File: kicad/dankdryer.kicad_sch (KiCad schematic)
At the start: 22 parts, among them J13 barreljack, J9 UART, SW2 boot, U1 AP63203WU, U6 ESP32-C6-MINI-1U

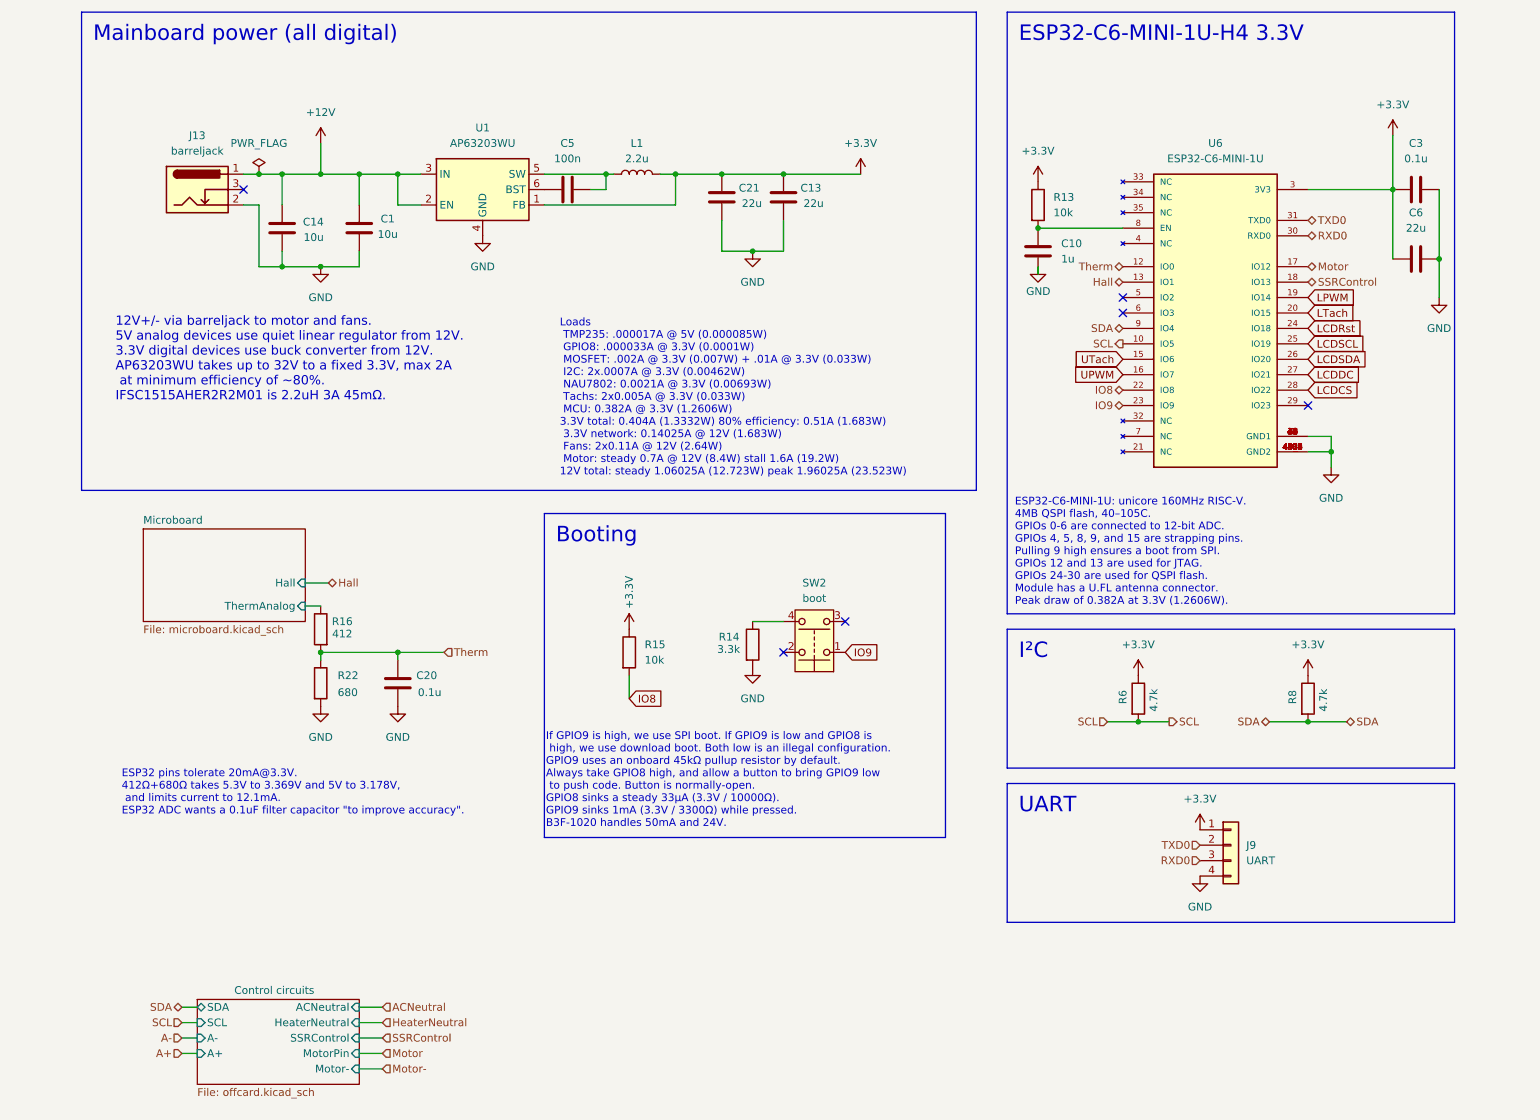
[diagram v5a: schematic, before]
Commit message: [pcb] don't run trace between connectors #97
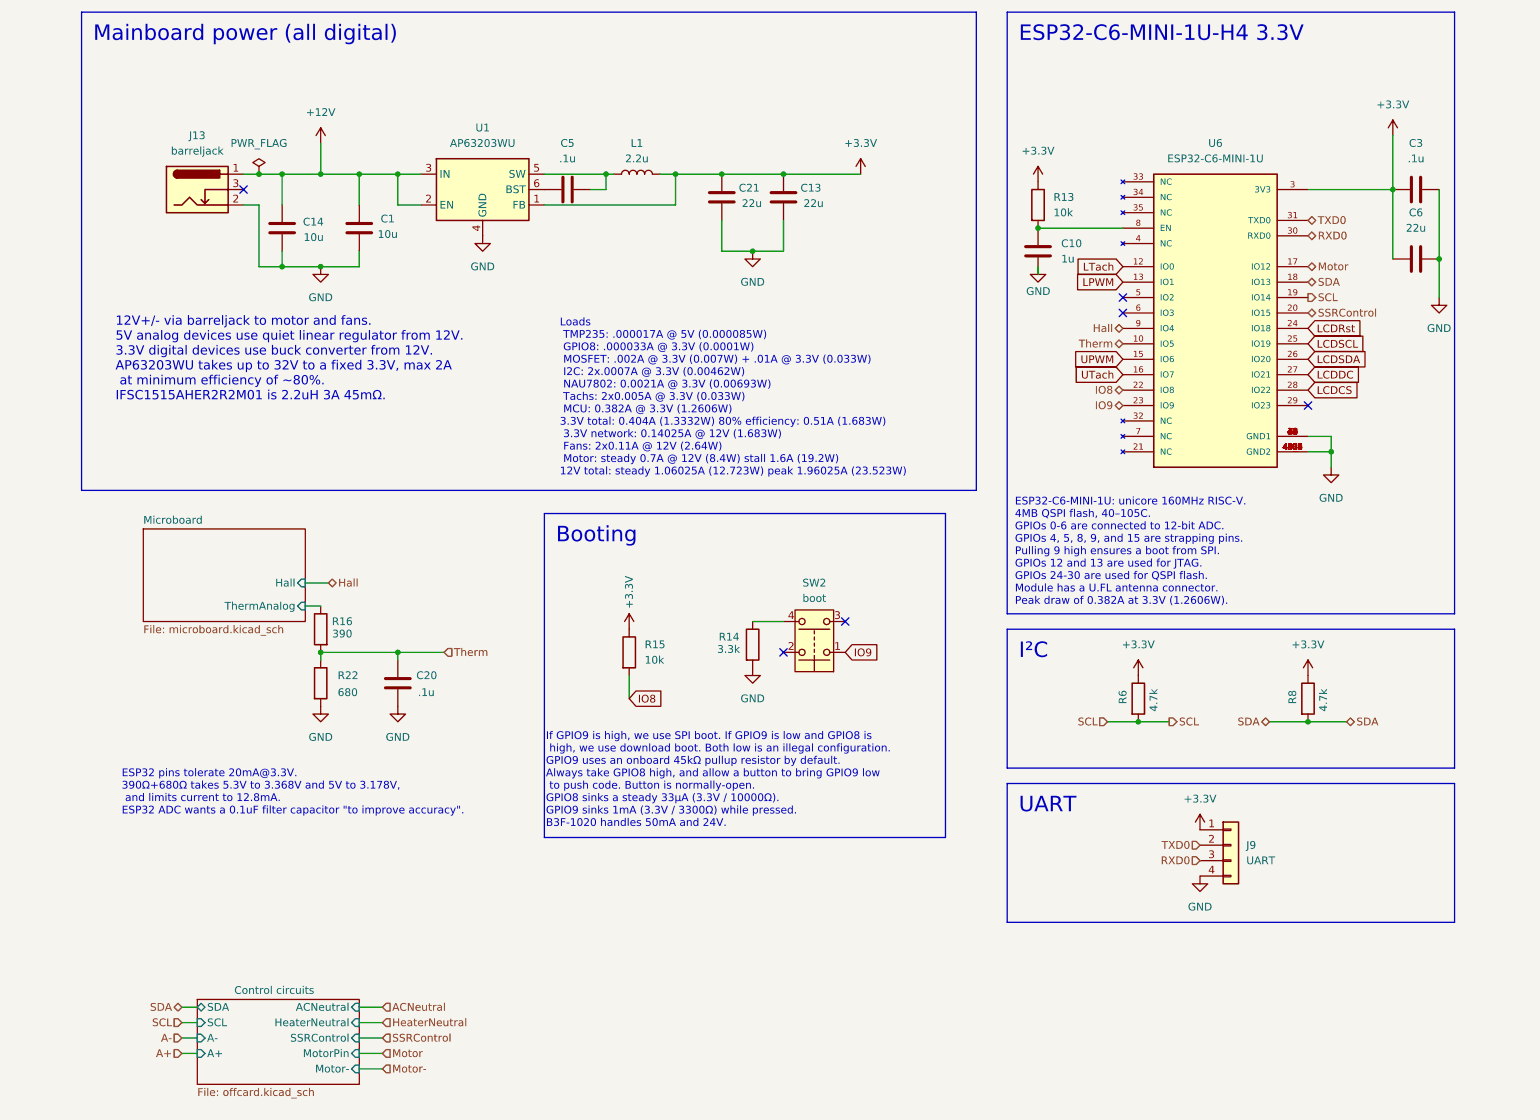
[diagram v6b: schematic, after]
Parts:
- C10, C6: footprint Capacitor_SMD:C_1206_3216Metric_Pad1.33x1.80mm_HandSolder -> Capacitor_SMD:C_0805_2012Metric_Pad1.18x1.45mm_HandSolder
- C20, C3: value 0.1u -> .1u; footprint Capacitor_SMD:C_1206_3216Metric_Pad1.33x1.80mm_HandSolder -> Capacitor_SMD:C_0805_2012Metric_Pad1.18x1.45mm_HandSolder
- C5: value 100n -> .1u
- R13, R22, R6, R8: footprint Resistor_SMD:R_1206_3216Metric_Pad1.30x1.75mm_HandSolder -> Resistor_SMD:R_0805_2012Metric_Pad1.20x1.40mm_HandSolder
- R16: value 412 -> 390; footprint Resistor_SMD:R_1206_3216Metric_Pad1.30x1.75mm_HandSolder -> Resistor_SMD:R_0805_2012Metric_Pad1.20x1.40mm_HandSolder
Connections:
- net Hall: now also U6.9 (IO4); no longer U6.13 (IO1)
- net LPWM: now also U6.13 (IO1); no longer U6.19 (IO14)
- net LTach: now also U6.12 (IO0); no longer U6.20 (IO15)
- net SCL: now also U6.19 (IO14); no longer U6.10 (IO5)
- net SDA: now also U6.18 (IO13); no longer U6.9 (IO4)
- net SSRControl: now also U6.20 (IO15); no longer U6.18 (IO13)
- net Therm: now also U6.10 (IO5); no longer U6.12 (IO0)
- net UPWM: now also U6.15 (IO6); no longer U6.16 (IO7)
- net UTach: now also U6.16 (IO7); no longer U6.15 (IO6)
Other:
- note added: "ESP32 pins tolerate 20mA@3.3V. 390Ω+680Ω takes 5.3V to 3.368V and 5V to 3.178V, and limits current to 12.8mA. ESP32 ADC wants a 0.1uF filter capacitor "to improve accuracy"."
- note removed: "ESP32 pins tolerate 20mA@3.3V. 412Ω+680Ω takes 5.3V to 3.369V and 5V to 3.178V, and limits current to 12.1mA. ESP32 ADC wants a 0.1uF filter capacitor "to improve accuracy"."
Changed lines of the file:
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@@
 		)
 	)
-	(text "ESP32 pins tolerate 20mA@3.3V.\n412Ω+680Ω takes 5.3V to 3.369V and 5V to 3.178V,\n and limits current to 12.1mA.\nESP32 ADC wants a 0.1uF filter capacitor \"to improve accuracy\"."
+	(text "ESP32 pins tolerate 20mA@3.3V.\n390Ω+680Ω takes 5.3V to 3.368V and 5V to 3.178V,\n and limits current to 12.8mA.\nESP32 ADC wants a 0.1uF filter capacitor \"to improve accuracy\"."
 		(exclude_from_sim no)
 		(at 24.384 143.764 0)
@@
 		)
 	)
-	(global_label "LCDSDA"
+	(global_label "UPWM"
 		(shape input)
-		(at 219.71 72.39 0)
+		(at 189.23 72.39 180)
 		(fields_autoplaced yes)
 		(effects
@@
 				(size 1.27 1.27)
 			)
-			(justify left)
+			(justify right)
 		)
 		(property "Intersheetrefs" "${INTERSHEET_REFS}"
-			(at 229.8314 72.39 0)
+			(at 180.7415 72.39 0)
 			(effects
 				(font
 					(size 1.27 1.27)
 				)
-				(justify left)
+				(justify right)
 				(hide yes)
 			)
 		)
 	)
-	(global_label "LCDSCL"
+	(global_label "LCDSDA"
 		(shape input)
-		(at 219.71 69.85 0)
+		(at 219.71 72.39 0)
 		(fields_autoplaced yes)
 		(effects
@@
 		)
 		(property "Intersheetrefs" "${INTERSHEET_REFS}"
-			(at 229.7709 69.85 0)
+			(at 229.8314 72.39 0)
 			(effects
 				(font
@@
 		)
 	)
-	(global_label "LCDRst"
+	(global_label "LPWM"
 		(shape input)
-		(at 219.71 67.31 0)
+		(at 189.23 59.69 180)
 		(fields_autoplaced yes)
 		(effects
@@
 				(size 1.27 1.27)
 			)
-			(justify left)
+			(justify right)
 		)
 		(property "Intersheetrefs" "${INTERSHEET_REFS}"
-			(at 229.2871 67.31 0)
+			(at 181.0439 59.69 0)
 			(effects
 				(font
 					(size 1.27 1.27)
 				)
-				(justify left)
+				(justify right)
 				(hide yes)
 			)
 		)
 	)
-	(global_label "LCDDC"
+	(global_label "LCDSCL"
 		(shape input)
-		(at 219.71 74.93 0)
+		(at 219.71 69.85 0)
 		(fields_autoplaced yes)
 		(effects
@@
 		)
 		(property "Intersheetrefs" "${INTERSHEET_REFS}"
-			(at 228.8033 74.93 0)
+			(at 229.7709 69.85 0)
 			(effects
 				(font
@@
 		)
 	)
-	(global_label "LTach"
+	(global_label "LCDCS"
 		(shape input)
-		(at 219.71 64.77 0)
+		(at 219.71 77.47 0)
 		(fields_autoplaced yes)
 		(effects
@@
 		)
 		(property "Intersheetrefs" "${INTERSHEET_REFS}"
-			(at 228.0775 64.77 0)
+			(at 228.7428 77.47 0)
 			(effects
 				(font
@@
 		)
 	)
-	(global_label "LCDCS"
+	(global_label "LCDRst"
 		(shape input)
-		(at 219.71 77.47 0)
+		(at 219.71 67.31 0)
 		(fields_autoplaced yes)
 		(effects
@@
 		)
 		(property "Intersheetrefs" "${INTERSHEET_REFS}"
-			(at 228.7428 77.47 0)
+			(at 229.2871 67.31 0)
 			(effects
 				(font
@@
 		)
 	)
-	(global_label "IO9"
+	(global_label "LCDDC"
 		(shape input)
-		(at 143.51 120.65 0)
+		(at 219.71 74.93 0)
 		(fields_autoplaced yes)
 		(effects
@@
 		)
 		(property "Intersheetrefs" "${INTERSHEET_REFS}"
-			(at 149.64 120.65 0)
+			(at 228.8033 74.93 0)
 			(effects
 				(font
@@
 		)
 	)
-	(global_label "UTach"
+	(global_label "IO9"
 		(shape input)
-		(at 189.23 72.39 180)
+		(at 143.51 120.65 0)
 		(fields_autoplaced yes)
 		(effects
@@
 				(size 1.27 1.27)
 			)
-			(justify right)
+			(justify left)
 		)
 		(property "Intersheetrefs" "${INTERSHEET_REFS}"
-			(at 180.5601 72.39 0)
+			(at 149.64 120.65 0)
 			(effects
 				(font
 					(size 1.27 1.27)
 				)
-				(justify right)
+				(justify left)
 				(hide yes)
 			)
 		)
 	)
-	(global_label "LPWM"
+	(global_label "LTach"
 		(shape input)
-		(at 219.71 62.23 0)
+		(at 189.23 57.15 180)
 		(fields_autoplaced yes)
 		(effects
@@
 				(size 1.27 1.27)
 			)
-			(justify left)
+			(justify right)
 		)
 		(property "Intersheetrefs" "${INTERSHEET_REFS}"
-			(at 227.8961 62.23 0)
+			(at 180.8625 57.15 0)
 			(effects
 				(font
 					(size 1.27 1.27)
 				)
-				(justify left)
+				(justify right)
 				(hide yes)
 			)
 		)
 	)
-	(global_label "IO8"
+	(global_label "UTach"
 		(shape input)
-		(at 107.95 128.27 0)
+		(at 189.23 74.93 180)
 		(fields_autoplaced yes)
 		(effects
@@
 				(size 1.27 1.27)
 			)
-			(justify left)
+			(justify right)
 		)
 		(property "Intersheetrefs" "${INTERSHEET_REFS}"
-			(at 114.08 128.27 0)
+			(at 180.5601 74.93 0)
 			(effects
 				(font
 					(size 1.27 1.27)
 				)
-				(justify left)
+				(justify right)
 				(hide yes)
 			)
 		)
 	)
-	(global_label "UPWM"
+	(global_label "IO8"
 		(shape input)
-		(at 189.23 74.93 180)
+		(at 107.95 128.27 0)
 		(fields_autoplaced yes)
 		(effects
@@
 				(size 1.27 1.27)
 			)
-			(justify right)
+			(justify left)
 		)
 		(property "Intersheetrefs" "${INTERSHEET_REFS}"
-			(at 180.7415 74.93 0)
+			(at 114.08 128.27 0)
 			(effects
 				(font
 					(size 1.27 1.27)
 				)
-				(justify right)
+				(justify left)
 				(hide yes)
 			)
@@
 		)
 	)
-	(hierarchical_label "SCL"
-		(shape output)
-		(at 189.23 69.85 180)
-		(effects
-			(font
-				(size 1.27 1.27)
-			)
-			(justify right)
-		)
-	)
 	(hierarchical_label "SDA"
 		(shape bidirectional)
@@
 		)
 	)
-	(hierarchical_label "SDA"
-		(shape bidirectional)
-		(at 189.23 67.31 180)
-		(effects
-			(font
-				(size 1.27 1.27)
-			)
-			(justify right)
-		)
-	)
 	(hierarchical_label "SCL"
 		(shape input)
@@
 		)
 	)
+	(hierarchical_label "Therm"
+		(shape bidirectional)
+		(at 189.23 69.85 180)
+		(effects
+			(font
+				(size 1.27 1.27)
+			)
+			(justify right)
+		)
+	)
 	(hierarchical_label "SCL"
 		(shape output)
@@
 		)
 	)
-	(hierarchical_label "SSRControl"
-		(shape bidirectional)
-		(at 219.71 59.69 0)
+	(hierarchical_label "SCL"
+		(shape output)
+		(at 219.71 62.23 0)
 		(effects
 			(font
@@
 		)
 	)
+	(hierarchical_label "Hall"
+		(shape bidirectional)
+		(at 189.23 67.31 180)
+		(effects
+			(font
+				(size 1.27 1.27)
+			)
+			(justify right)
+		)
+	)
 	(hierarchical_label "Therm"
 		(shape input)
@@
 		)
 	)
-	(hierarchical_label "Hall"
-		(shape bidirectional)
-		(at 189.23 59.69 180)
-		(effects
-			(font
-				(size 1.27 1.27)
-			)
-			(justify right)
-		)
-	)
 	(hierarchical_label "Motor"
 		(shape input)
@@
 		)
 	)
+	(hierarchical_label "SSRControl"
+		(shape bidirectional)
+		(at 219.71 64.77 0)
+		(effects
+			(font
+				(size 1.27 1.27)
+			)
+			(justify left)
+		)
+	)
 	(hierarchical_label "A+"
 		(shape input)
@@
 		)
 	)
-	(hierarchical_label "Therm"
+	(hierarchical_label "SDA"
 		(shape bidirectional)
-		(at 189.23 57.15 180)
+		(at 219.71 59.69 0)
 		(effects
 			(font
 				(size 1.27 1.27)
 			)
-			(justify right)
+			(justify left)
 		)
 	)
@@
 			)
 		)
-		(property "Value" "100n"
+		(property "Value" ".1u"
 			(at 97.79 39.37 90)
 			(effects
@@
 			)
 		)
-		(property "Footprint" "Resistor_SMD:R_1206_3216Metric_Pad1.30x1.75mm_HandSolder"
+		(property "Footprint" "Resistor_SMD:R_0805_2012Metric_Pad1.20x1.40mm_HandSolder"
 			(at 173.482 46.99 90)
 			(effects
@@
 			)
 		)
-		(property "Value" "0.1u"
+		(property "Value" ".1u"
 			(at 73.152 127.254 0)
 			(effects
@@
 			)
 		)
-		(property "Footprint" "Capacitor_SMD:C_1206_3216Metric_Pad1.33x1.80mm_HandSolder"
+		(property "Footprint" "Capacitor_SMD:C_0805_2012Metric_Pad1.18x1.45mm_HandSolder"
 			(at 70.8152 129.54 0)
 			(effects
@@
 			)
 		)
-		(property "Value" "412"
+		(property "Value" "390"
 			(at 60.706 117.602 0)
 			(effects
@@
 			)
 		)
-		(property "Footprint" "Resistor_SMD:R_1206_3216Metric_Pad1.30x1.75mm_HandSolder"
+		(property "Footprint" "Resistor_SMD:R_0805_2012Metric_Pad1.20x1.40mm_HandSolder"
 			(at 58.928 116.84 90)
 			(effects
@@
 			)
 		)
-		(property "Footprint" "Capacitor_SMD:C_1206_3216Metric_Pad1.33x1.80mm_HandSolder"
+		(property "Footprint" "Capacitor_SMD:C_0805_2012Metric_Pad1.18x1.45mm_HandSolder"
 			(at 176.2252 58.42 0)
 			(effects
@@
 			)
 		)
-		(property "Footprint" "Resistor_SMD:R_1206_3216Metric_Pad1.30x1.75mm_HandSolder"
+		(property "Footprint" "Resistor_SMD:R_0805_2012Metric_Pad1.20x1.40mm_HandSolder"
 			(at 217.932 128.27 90)
 			(effects
@@
 			)
 		)
-		(property "Footprint" "Capacitor_SMD:C_1206_3216Metric_Pad1.33x1.80mm_HandSolder"
+		(property "Footprint" "Capacitor_SMD:C_0805_2012Metric_Pad1.18x1.45mm_HandSolder"
 			(at 233.68 56.8452 0)
 			(effects
@@
 			)
 		)
-		(property "Footprint" "Resistor_SMD:R_1206_3216Metric_Pad1.30x1.75mm_HandSolder"
+		(property "Footprint" "Resistor_SMD:R_0805_2012Metric_Pad1.20x1.40mm_HandSolder"
 			(at 55.372 125.73 90)
 			(effects
@@
 			)
 		)
-		(property "Footprint" "Resistor_SMD:R_1206_3216Metric_Pad1.30x1.75mm_HandSolder"
+		(property "Footprint" "Resistor_SMD:R_0805_2012Metric_Pad1.20x1.40mm_HandSolder"
 			(at 189.992 128.27 90)
 			(effects
@@
 			)
 		)
-		(property "Value" "0.1u"
+		(property "Value" ".1u"
 			(at 237.49 39.37 90)
 			(effects
@@
 			)
 		)
-		(property "Footprint" "Capacitor_SMD:C_1206_3216Metric_Pad1.33x1.80mm_HandSolder"
+		(property "Footprint" "Capacitor_SMD:C_0805_2012Metric_Pad1.18x1.45mm_HandSolder"
 			(at 241.3 43.4848 0)
 			(effects

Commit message: [pcb] drop voltage divider off LM35 output
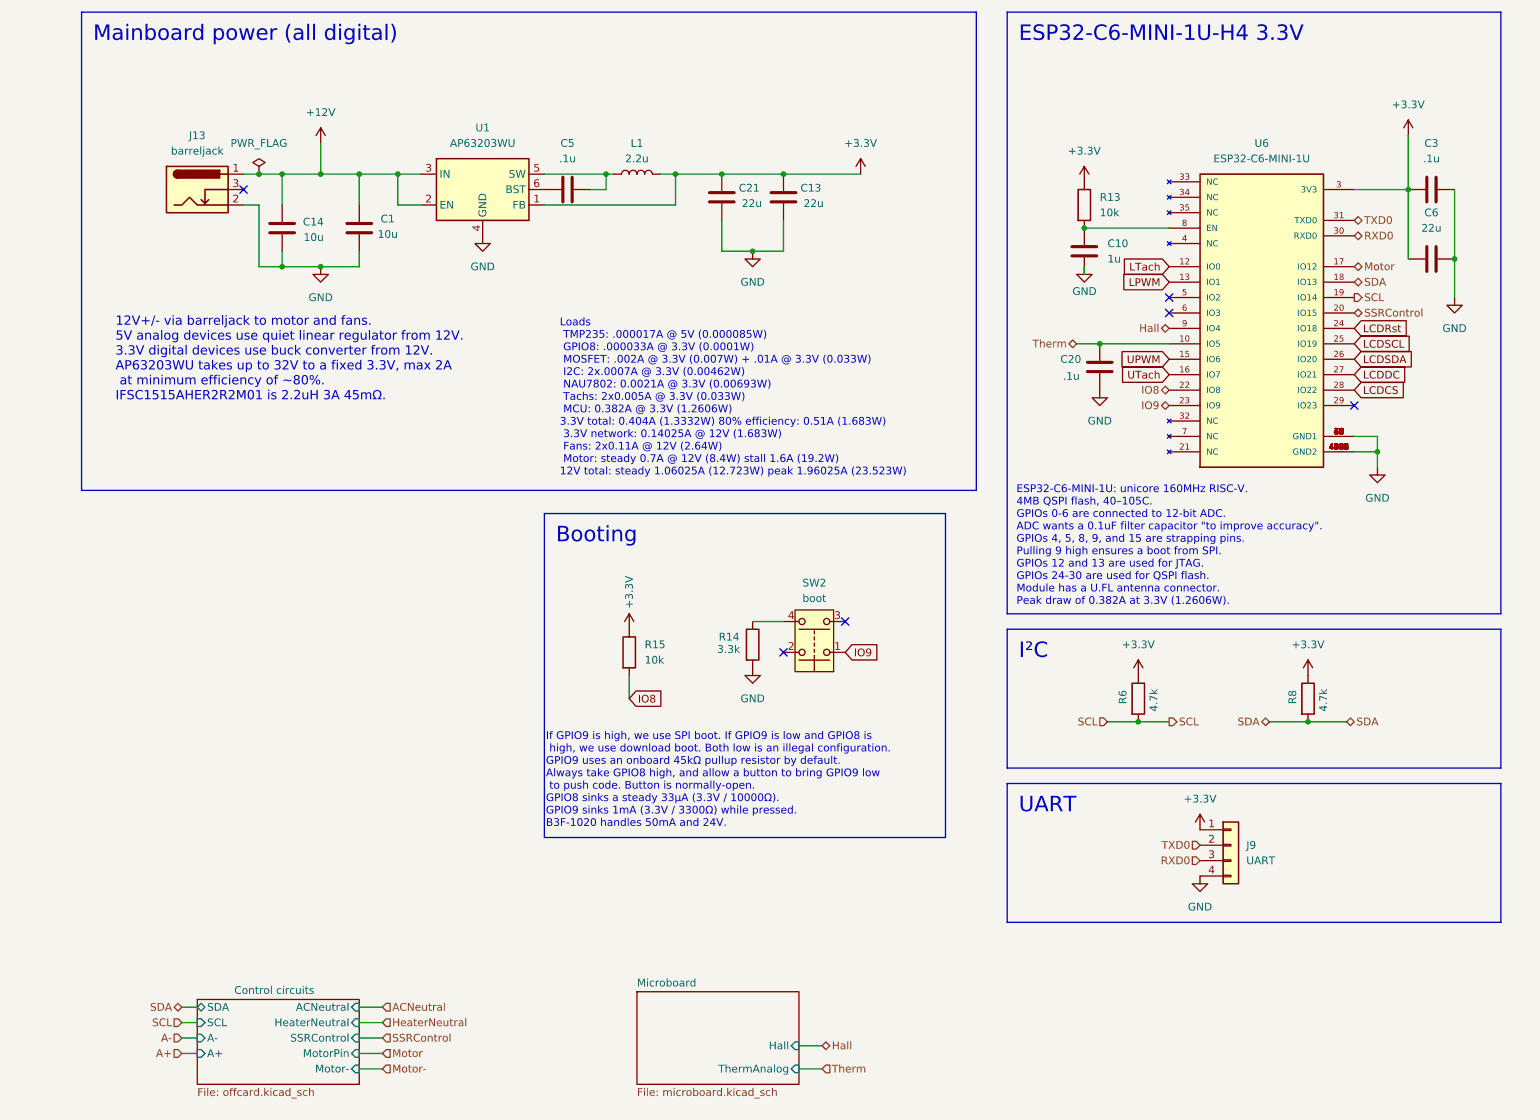
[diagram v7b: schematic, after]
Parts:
- removed R16: 390, Resistor_SMD:R_0805_2012Metric_Pad1.20x1.40mm_HandSolder, symbol Device:R
- removed R22: 680, Resistor_SMD:R_0805_2012Metric_Pad1.20x1.40mm_HandSolder, symbol Device:R
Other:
- note added: "ESP32-C6-MINI-1U: unicore 160MHz RISC-V. 4MB QSPI flash, 40–105C. GPIOs 0-6 are connected to 12-bit ADC. ADC wants a 0.1uF filter capacitor "to improve accuracy". GPIOs 4, 5, 8, 9, and 15 are strapping pins. Pulling 9 high ensures a boot from SPI. GPIOs 12 and 13 are used for JTAG. GPIOs 24-30 are used for QSPI flash. Module has a U.FL antenna connector. Peak draw of 0.382A at 3.3V (1.2606W)."
- note removed: "ESP32 pins tolerate 20mA@3.3V. 390Ω+680Ω takes 5.3V to 3.368V and 5V to 3.178V, and limits current to 12.8mA. ESP32 ADC wants a 0.1uF filter capacitor "to improve accuracy"."
- note removed: "ESP32-C6-MINI-1U: unicore 160MHz RISC-V. 4MB QSPI flash, 40–105C. GPIOs 0-6 are connected to 12-bit ADC. GPIOs 4, 5, 8, 9, and 15 are strapping pins. Pulling 9 high ensures a boot from SPI. GPIOs 12 and 13 are used for JTAG. GPIOs 24-30 are used for QSPI flash. Module has a U.FL antenna connector. Peak draw of 0.382A at 3.3V (1.2606W)."
- moved on the sheet: C10, C20, C3, C6, R13, U6
